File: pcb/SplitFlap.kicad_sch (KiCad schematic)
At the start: 17 parts, among them U1 PCF8575DBR, U2 ULN2003

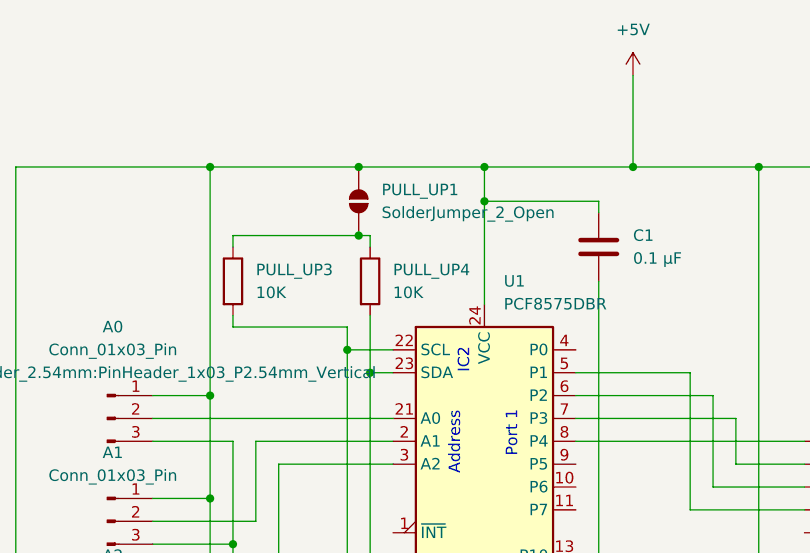
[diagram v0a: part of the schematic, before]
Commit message: Remove data line pull-ups
The SCL and SDL pull-ups need to happen on 3.3v, yet in the current
design they are attached to the 5v line.  Since they are only necessary
once per circuit (8 boards + esp32) I will leave them out of the board
design.
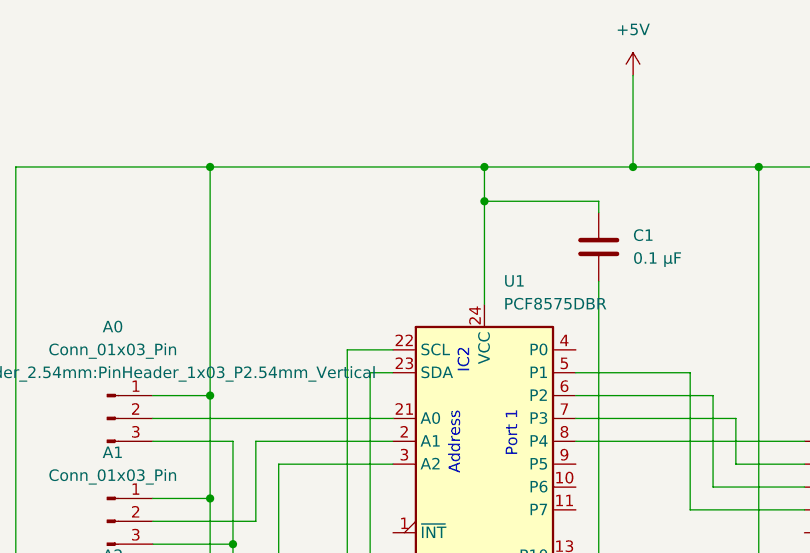
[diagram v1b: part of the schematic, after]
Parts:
- removed PULL_UP1: SolderJumper_2_Open, Jumper:SolderJumper-2_P1.3mm_Open_RoundedPad1.0x1.5mm, symbol Jumper:SolderJumper_2_Open
- removed PULL_UP3, PULL_UP4: 10K, Resistor_SMD:R_0603_1608Metric, symbol Device:R
